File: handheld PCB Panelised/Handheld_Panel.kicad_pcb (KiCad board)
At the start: 2 copper layers, 337.8 x 95.8 mm, 88 parts, among them J1 Conn_02x20_Odd_Even, J10 Connector Left Board, J11 Connector Right Board, J12 Connector Right Board, J13 Connector Left Board, J2 TP4056_Module, J3 Joystick_Left, J4 Joystick_Right, J5 Display_5V, J6 Speaker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

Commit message: added art on my PCB including a capybara and a horse that i drew myself!!!
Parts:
- removed the G*** at (497.8, 92.3)
- removed the G*** at (396.7, 94.4)
- added G***: LOGO, LOGO, F.Cu at (341.8, 42.4)
- added G***: LOGO, LOGO, F.Cu at (269.0, 57.9)
- added G***: LOGO, LOGO, F.Cu at (385.8, 66.6)
- added G***: LOGO, LOGO, F.Cu at (485.0, 46.4)
- added G***: LOGO, LOGO, F.Cu at (310.3, 89.1)
- added G***: LOGO, LOGO, F.Cu at (419.8, 63.2)
- added G***: LOGO, LOGO, F.Cu at (569.1, 84.5)
- added G***: LOGO, LOGO, F.Cu at (418.0, 97.4)

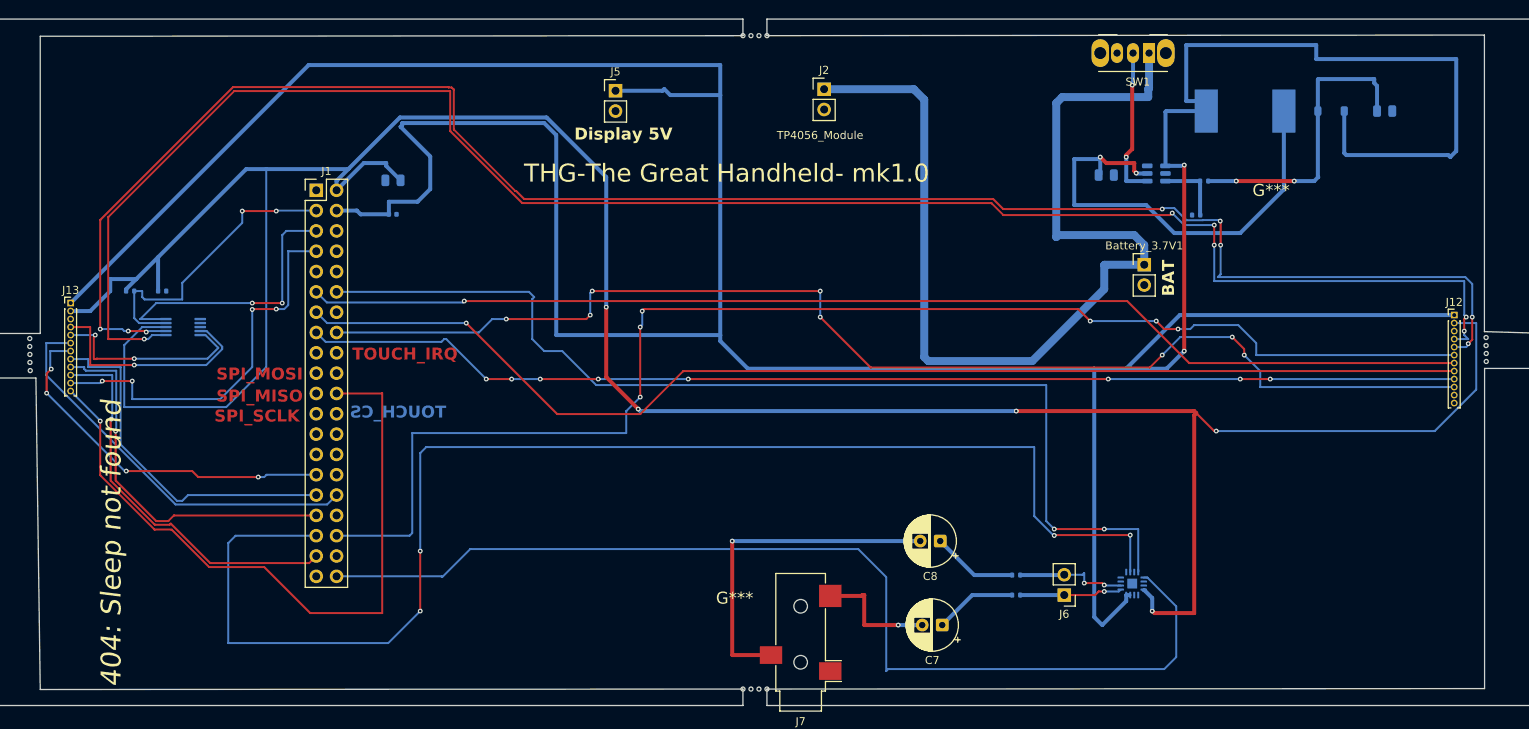
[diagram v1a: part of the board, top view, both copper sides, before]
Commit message: fixed the orientation of the pcb art
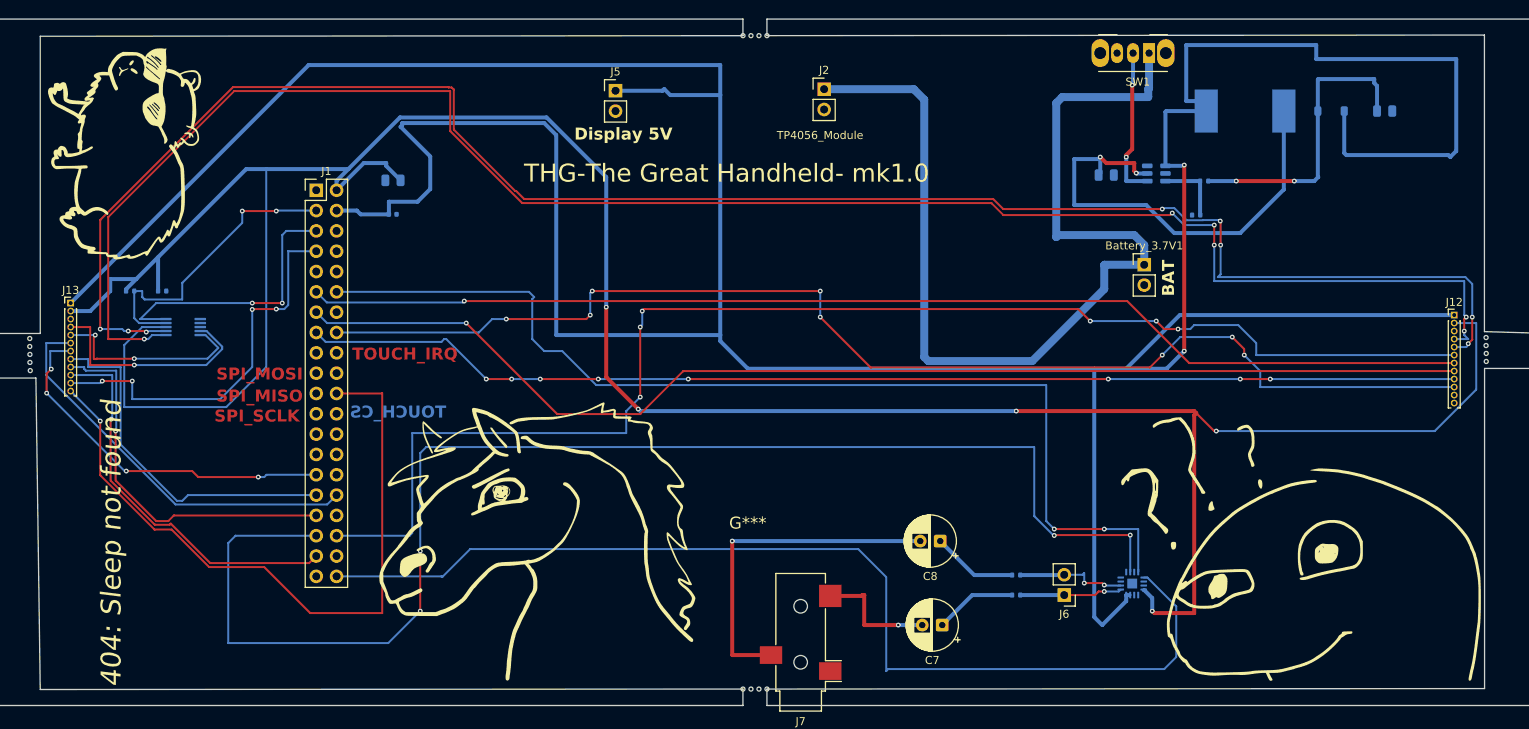
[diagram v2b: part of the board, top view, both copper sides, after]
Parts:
- removed the G*** at (341.8, 42.4)
- removed the G*** at (385.8, 66.6)
- removed the G*** at (485.0, 46.4)
- removed the G*** at (419.8, 63.2)
- removed the G*** at (418.0, 97.4)
- added G***: LOGO, LOGO, F.Cu at (419.6, 88.0)
- added G***: LOGO, LOGO, F.Cu at (392.3, 90.4)
- added G***: LOGO, LOGO, F.Cu at (342.0, 42.4)
- added G***: LOGO, LOGO, F.Cu at (488.6, 91.8)

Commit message: finally fixed the art on the PCB
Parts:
- removed the G*** at (419.6, 88.0)
- removed the G*** at (269.0, 57.9)
- removed the G*** at (569.1, 84.5)
- added G***: LOGO, LOGO, F.Cu at (266.3, 66.8)
- added G***: LOGO, LOGO, F.Cu at (574.4, 74.7)
- added g: LOGO, LOGO, F.Cu at (412.1, 93.5)

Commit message: ok this time i finally fixed it with the mountains art on the back.
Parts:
- G*** (x2), g: moved to B.Cu
- moved G*** 41.7 mm to (307.9, 69.0)
- moved G*** 39.0 mm to (535.5, 72.7)
- moved g 15.8 mm to (427.4, 89.6), turned to 180 degrees
- moved G*** 0.34 mm to (310.4, 89.4)

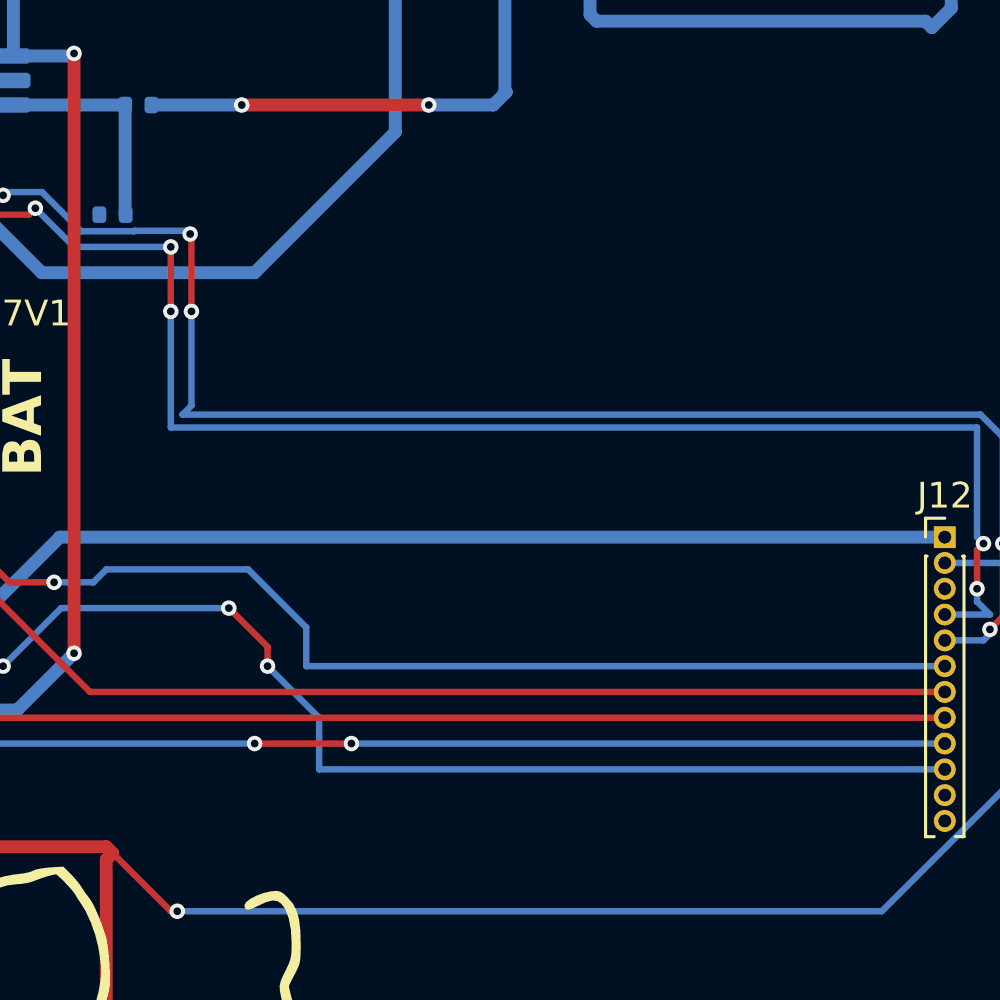
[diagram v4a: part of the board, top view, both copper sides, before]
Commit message: last time i forgot to add the qr code on the PCB now it is there!!
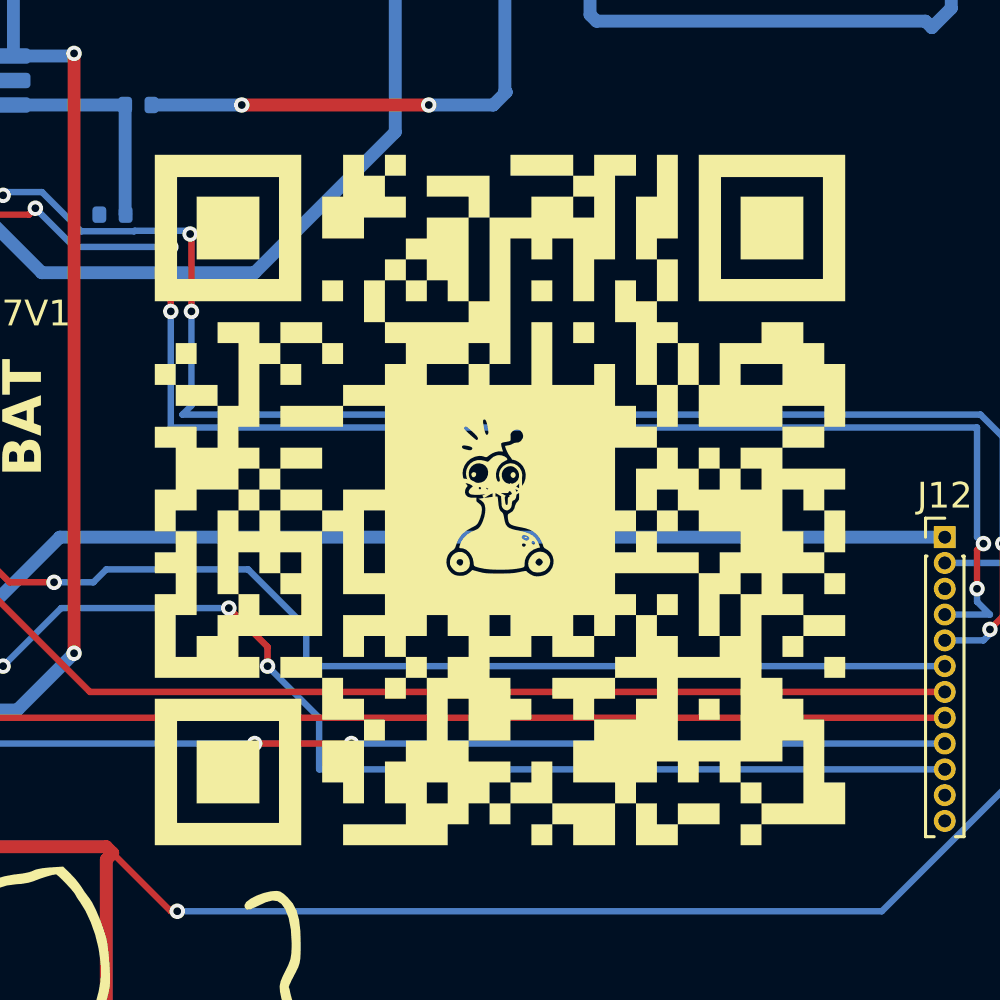
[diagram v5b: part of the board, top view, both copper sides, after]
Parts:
- added G***: LOGO, LOGO, F.Cu at (490.7, 60.6)
- moved G*** 41.5 mm to (266.4, 69.1), turned to 90 degrees
- moved G*** 40.0 mm to (574.7, 64.6), turned to -90 degrees
